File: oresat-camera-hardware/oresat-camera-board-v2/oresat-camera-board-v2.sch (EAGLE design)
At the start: 43 parts, among them J1 4-1734742-0, U1 AR0134CSSM00SPCA0, U2 TPS70618DRVR, U3 TPS71928-28DRVT, U4 TPS71928-28DRVT, X1 KC2520B27.0000C10E00

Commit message: more cleanup
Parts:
- J1: value 4-1734742-0 -> 3-1734742-6; device J-TEConnectivity-4-1734742-0:4-1734742-0 -> J-TEConnectivity-3-1734742-6 :3-1734742-6
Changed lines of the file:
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@@
 <part name="SUPPLY2" library="SparkFun-PowerSymbols" deviceset="3.3V" device=""/>
 <part name="GND5" library="SparkFun-PowerSymbols" deviceset="GND" device=""/>
-<part name="J1" library="J-TEConnectivity-4-1734742-0" deviceset="4-1734742-0" device=""/>
+<part name="J1" library="J-TEConnectivity-3-1734742-6 " deviceset="3-1734742-6" device=""/>
 <part name="U1" library="U-ONSemi-AR0134" deviceset="AR0134CSSM00SPCA0" device=""/>
 <part name="GND6" library="SparkFun-PowerSymbols" deviceset="GND" device=""/>

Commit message: made a few minor adjustments when I was making the BOMs
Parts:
- R5: value 10K -> 10k
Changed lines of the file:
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@@
 <?xml version="1.0" encoding="utf-8"?>
 <!DOCTYPE eagle SYSTEM "eagle.dtd">
-<eagle version="9.4.2">
+<eagle version="9.5.0">
 <drawing>
 <settings>
@@
 <part name="C7" library="oresat-rcl" deviceset="C-EU" device="0603-C-NOSILK" value="2.2uF"/>
 <part name="C14" library="oresat-rcl" deviceset="C-EU" device="0603-C-NOSILK" value="1.0uF"/>
-<part name="R5" library="oresat-rcl" deviceset="R-US_" device="0402-B-NOSILK" value="10K"/>
+<part name="R5" library="oresat-rcl" deviceset="R-US_" device="0402-B-NOSILK" value="10k"/>
 <part name="SUPPLY9" library="SparkFun-PowerSymbols" deviceset="3.3V" device=""/>
 <part name="GND7" library="SparkFun-PowerSymbols" deviceset="GND" device=""/>

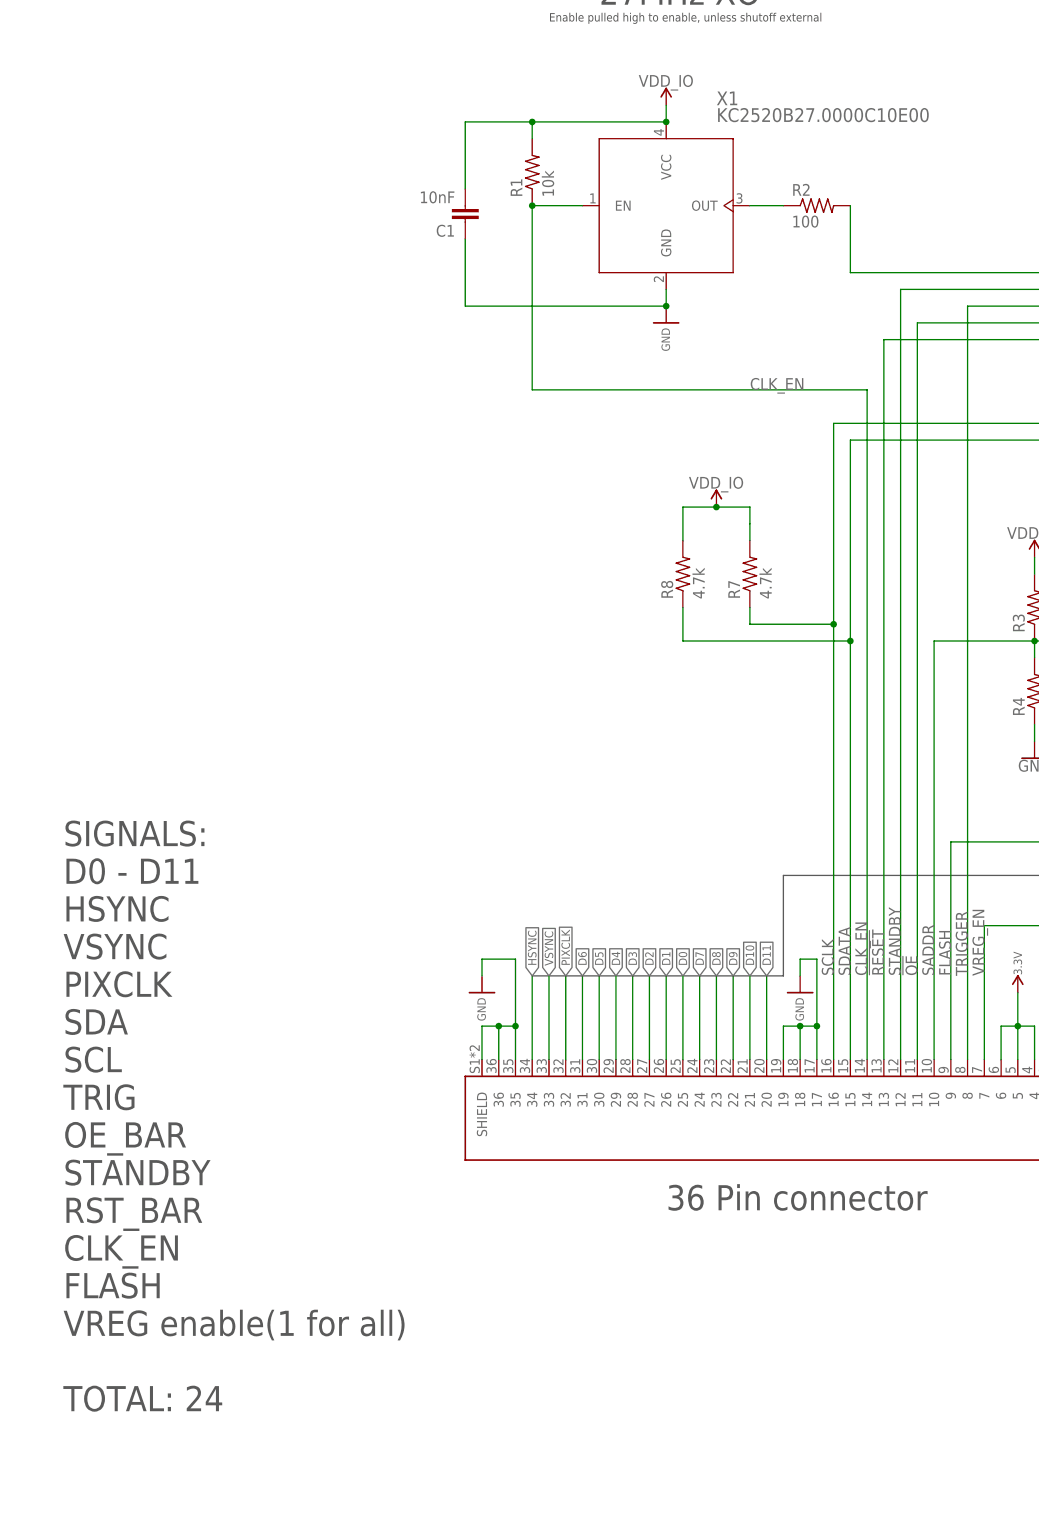
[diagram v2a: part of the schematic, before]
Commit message: mostly finished implementing v0 changes, but have a few more to go
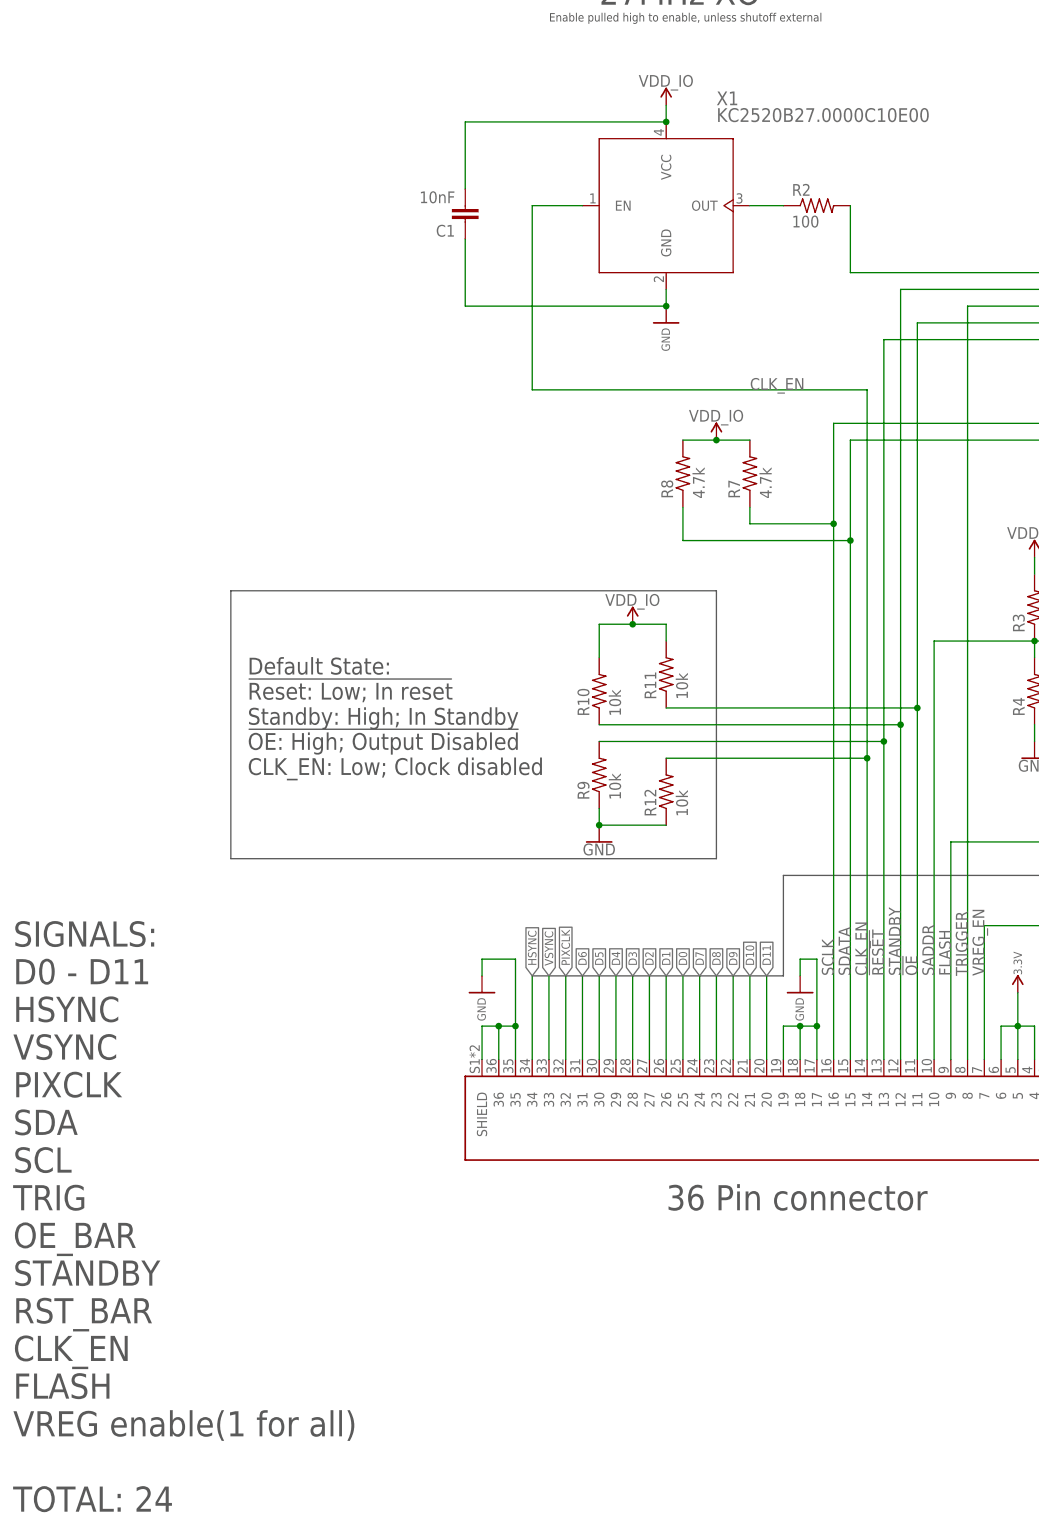
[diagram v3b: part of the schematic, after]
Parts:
- removed R1: 10k, oresat-rcl:R-US_0402-B
- added R10, R11, R12, R9: 10k, oresat-rcl:R-US_0402-B
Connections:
- net !OE: now also R11.1
- net !RESET: now also R9.2
- net CLK_EN: now also R12.2; no longer R1.1
- net GND: now also R12.1, R9.1
- net STANDBY: now also R10.1
- net VDD_IO: now also R10.2, R11.2; no longer R1.2
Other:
- note added: "Default State: !Reset: Low; In reset Standby: High; In Standby !OE: High; Output Disabled CLK_EN: Low; Clock disabled"
- moved on the sheet: R7, R8
